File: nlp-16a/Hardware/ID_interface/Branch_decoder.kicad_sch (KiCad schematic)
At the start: 32 parts

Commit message: 命令デコーダインターフェイスだいたい完了！！
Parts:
- removed U? (x16): CD74HC00, Package_DIP:DIP-14_W7.62mm, symbol CD74HCxx:CD74HC00
- added U16, U17, U18, U21: CD74HC00, Package_DIP:DIP-14_W7.62mm, symbol CD74HCxx:CD74HC00
- gave numbers to parts that had none: 4
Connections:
- net Flag_C: now also U21.13
- net Flag_V: now also U21.2
- net Flag_Z: now also U20.13; no longer U20.2
- net Flag_mode0: now also U19.1, U19.5; no longer U19.2, U19.2
- net Flag_mode1: now also U22.4, U22.5, U17.1; no longer U22.1, U22.2
- net Flag_mode2: now also U16.1
- net Flag_mode3: now also U15.5, U16.5, U17.5, U18.5; no longer U15.2
- net GND: now also U16.7 (GND), U16.7 (GND), U16.7 (GND), U16.7 (GND), U17.7 (GND), U17.7 (GND), U17.7 (GND), U17.7 (GND), U18.7 (GND), U18.7 (GND), U18.7 (GND), U18.7 (GND), U21.7 (GND), U21.7 (GND), U21.7 (GND), U21.7 (GND); no longer U22.1, U22.2
- net VCC: now also U16.14 (VCC), U16.14 (VCC), U16.14 (VCC), U16.14 (VCC), U17.14 (VCC), U17.14 (VCC), U17.14 (VCC), U17.14 (VCC), U18.14 (VCC), U18.14 (VCC), U18.14 (VCC), U18.14 (VCC), U21.14 (VCC), U21.14 (VCC), U21.14 (VCC), U21.14 (VCC)
- net at U20.1: now also U15.8; no longer U15.3
- net at U22.3: now also U17.2, U18.1
- net at U20.3: now also U20.4; no longer U20.1
- removed net ~NOP: U19.3
- new net: U19.8, U22.10, U22.9
- new net: U21.10, U21.6, U21.9
- new net: U21.8, U22.13
- new net: U15.10, U15.6, U15.9
- new net: U20.10, U20.6, U20.9
- new net: U20.8, U22.12
- new net: U15.11, U15.4
- new net: U15.12, U15.13, U15.3
- new net: U17.8, U21.1
- new net: U21.3, U21.4
- new net: U18.11, U18.4
- new net: U18.10, U18.6, U18.9
- new net: U18.12, U18.13, U18.3
- new net: U19.10, U19.11
- new net: U19.6, U19.9
- new net: U16.2, U18.2, U22.6
- new net: U19.12, U19.3, U19.4
- new net: U19.13, U19.2, U22.11
- new net: U18.8, U21.12
- new net: U17.11, U17.4
- new net: U17.10, U17.6, U17.9
- new net: U21.11, U21.5
- new net: U20.11, U20.5
- new net: U16.8, U20.12
- new net: U16.11, U16.4
- new net: U16.12, U16.13, U16.3
- new net: U16.10, U16.6, U16.9
- new net: U17.12, U17.13, U17.3
- new net NOP: U22.8
- no-connect marks 1 -> 0
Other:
- moved on the sheet: U22C, U22D

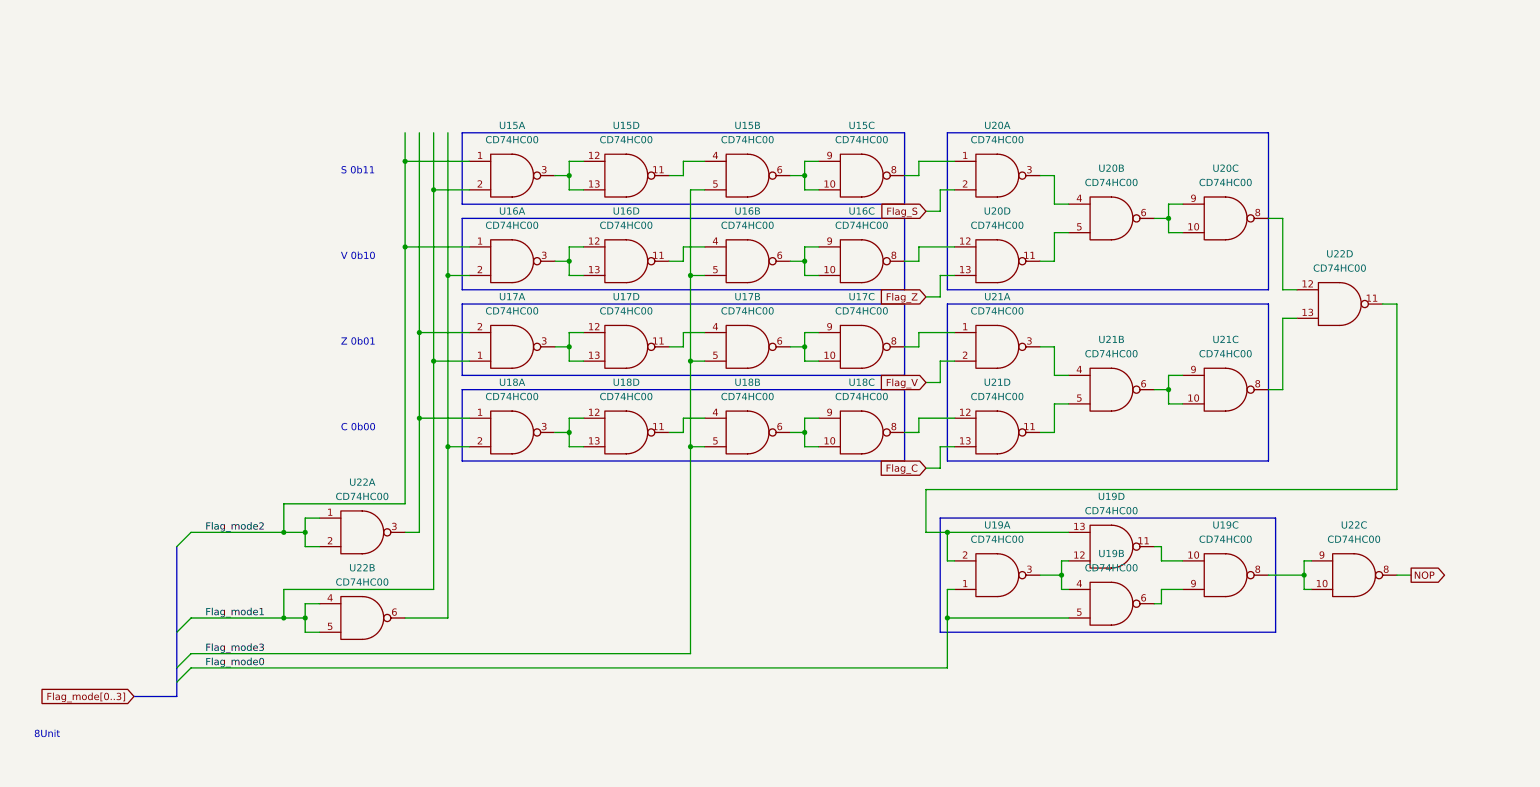
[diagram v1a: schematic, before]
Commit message: v1.1全ガーバーを更新
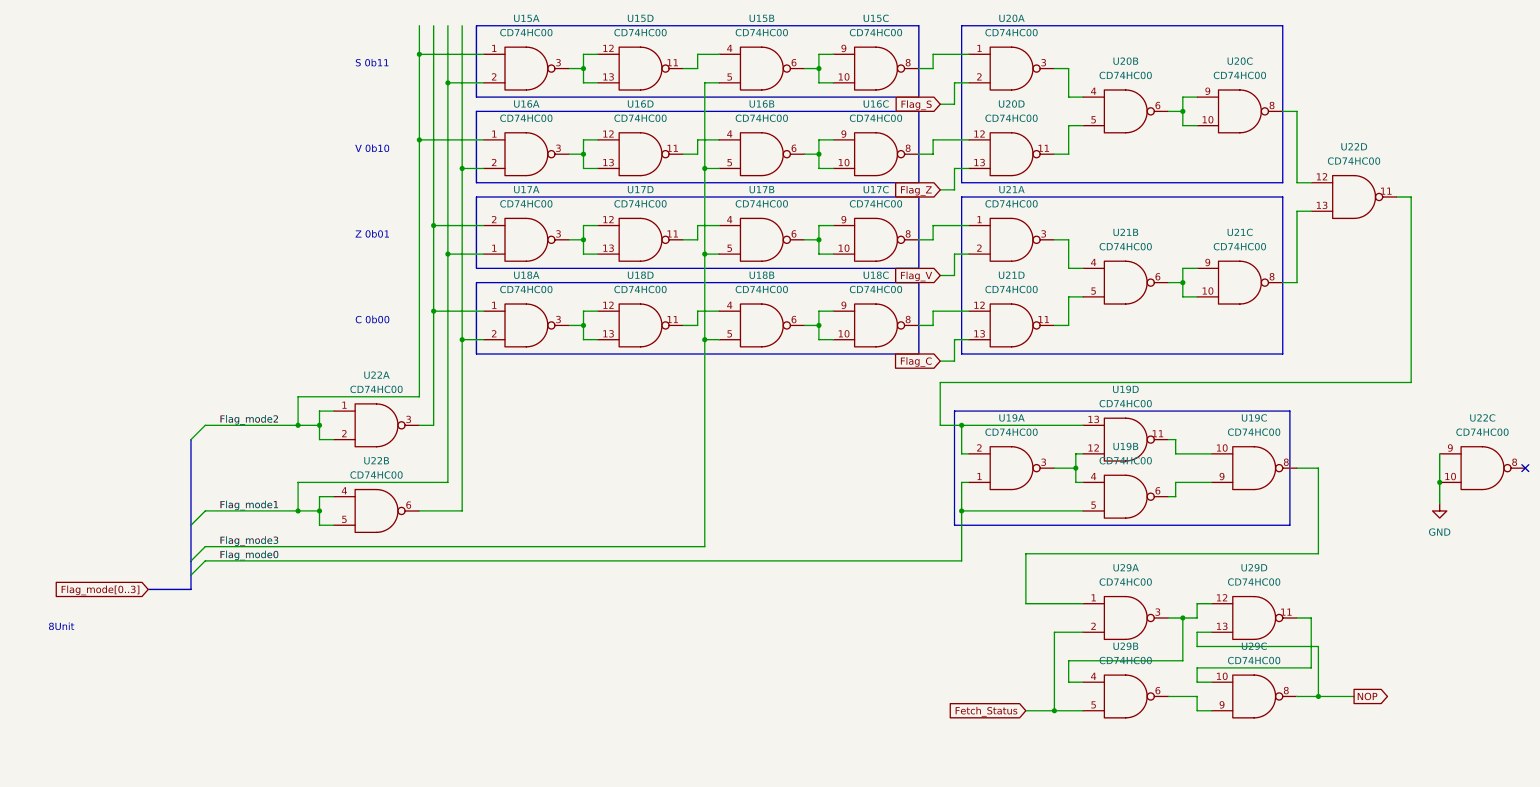
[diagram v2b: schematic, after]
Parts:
- added U29: CD74HC00, Package_DIP:DIP-14_W7.62mm, symbol CD74HCXX:CD74HC00
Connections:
- net GND: now also U22.10, U22.9, U29.7 (GND), U29.7 (GND), U29.7 (GND), U29.7 (GND)
- net NOP: now also U29.13, U29.8; no longer U22.8
- net VCC: now also U29.14 (VCC), U29.14 (VCC), U29.14 (VCC), U29.14 (VCC)
- new net: U29.12, U29.3, U29.4
- new net: U29.6, U29.9
- new net: U19.8, U29.1
- new net: U29.10, U29.11
- new net Fetch_Status: U29.2, U29.5
- no-connect marks 0 -> 1
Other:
- moved on the sheet: U15A, U15B, U15C, U15D, U16A, U16B, U16C, U16D, U17A, U17B, U17C, U17D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
